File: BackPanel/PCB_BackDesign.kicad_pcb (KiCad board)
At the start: 2 copper layers, 62.5 x 32 mm, 28 parts, among them J1 Molex Picoblade 0530470810, J2 Molex Picoblade 0530470910, J3 B2B-PH-K-S, J4 B2B-PH-K-S, SW1 KS11R23CQD (red), SW2 KS11R22CQD (black), SW3 KS11R27CQD (blue)

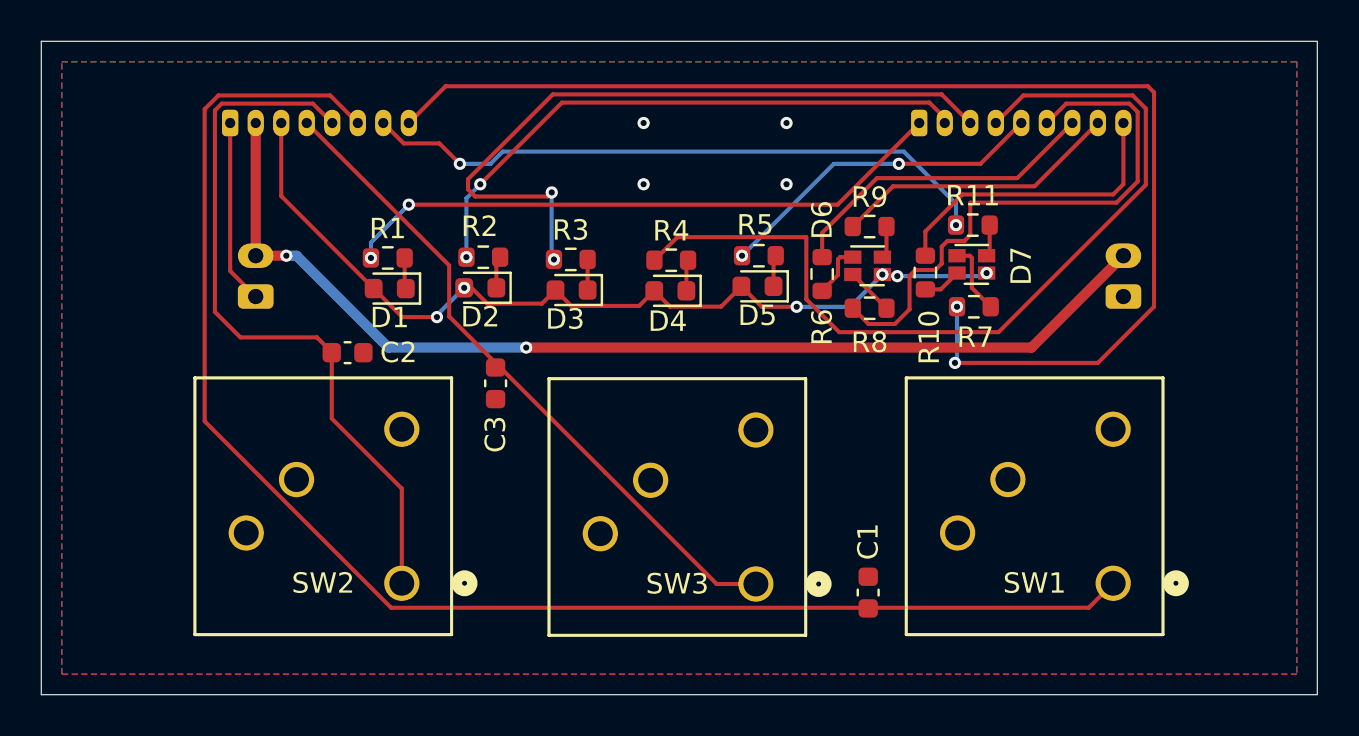
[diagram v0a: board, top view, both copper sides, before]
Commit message: Readded the mounting holes which mysteriously went missing;
updated the project to KiCAD 9.0 because I am silly.
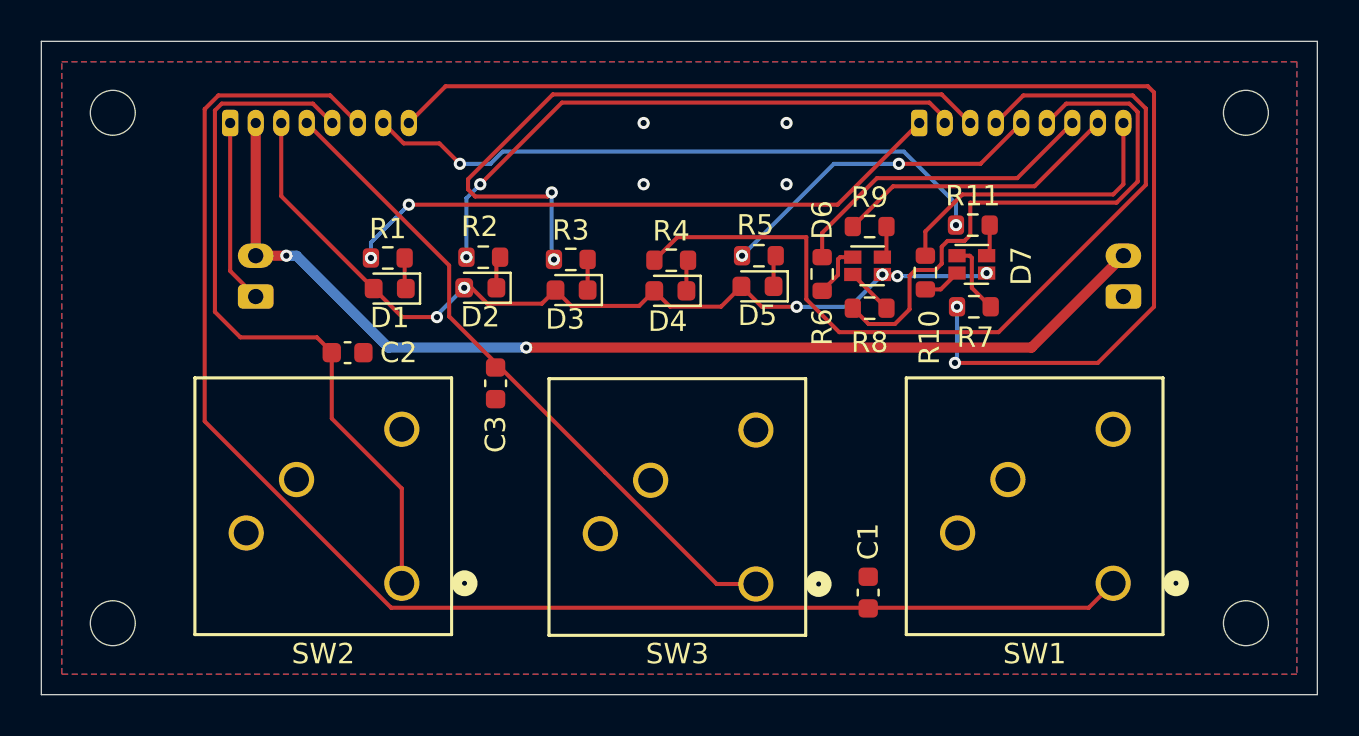
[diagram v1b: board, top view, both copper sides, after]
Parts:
- added REF**: MountingHole_2.2mm_M2, MountingHole:MountingHole_2.2mm_M2, F.Cu at (168.5, 95.5)
- added REF**: MountingHole_2.2mm_M2, MountingHole:MountingHole_2.2mm_M2, F.Cu at (168.5, 70.5)
- added REF**: MountingHole_2.2mm_M2, MountingHole:MountingHole_2.2mm_M2, F.Cu at (113.0, 70.5)
- added REF**: MountingHole_2.2mm_M2, MountingHole:MountingHole_2.2mm_M2, F.Cu at (113.0, 95.5)
